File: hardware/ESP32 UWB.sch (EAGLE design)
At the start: 55 parts, among them J2 HEADER-12P-2.54, J4 10118194-0001LF, Q3 S8050, Q4 S8050, U1 SILICON_LABS_CP2102N-A01-GQFN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, U2 V_REG_MIC2920, U5 DWM1000, U6 ESP32-C3-MINI-1-N4

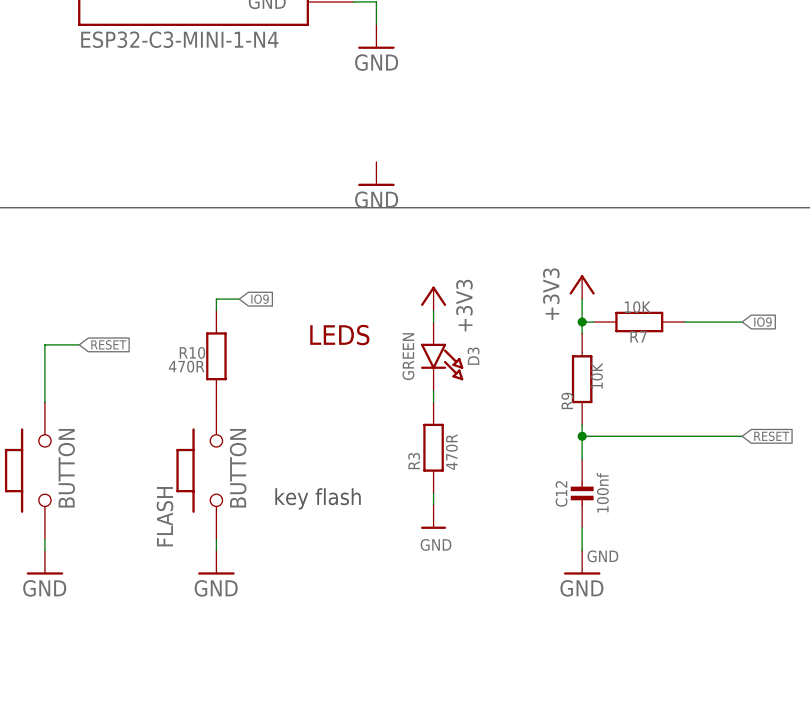
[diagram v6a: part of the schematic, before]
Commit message: fixed device prefixes, removed duplicate supply symbols
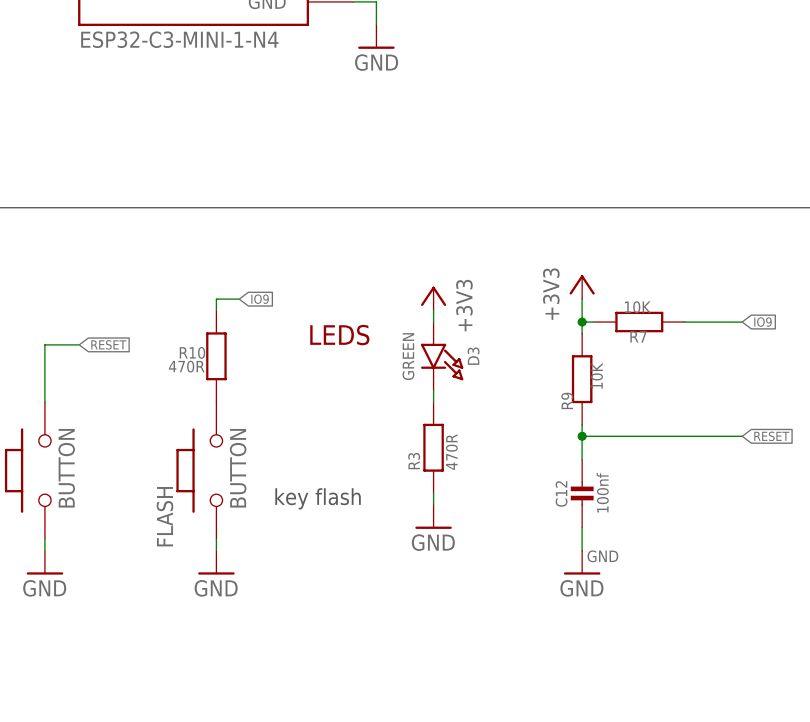
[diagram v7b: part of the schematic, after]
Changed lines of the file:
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@@
 <part name="+3V7" library="supply1" deviceset="+3V3" device=""/>
 <part name="+3V9" library="supply1" deviceset="+3V3" device=""/>
-<part name="GND13" library="supply1" deviceset="GND" device=""/>
 <part name="R18" library="isystems" deviceset="RESISTOR" device="0603" value="NC"/>
 <part name="R19" library="isystems" deviceset="RESISTOR" device="0603" value="NC"/>
@@
 <part name="GND29" library="supply1" deviceset="GND" device=""/>
 <part name="+3V4" library="supply1" deviceset="+3V3" device=""/>
-<part name="U$3" library="microbuilder" deviceset="GND" device=""/>
+<part name="U$3" library="supply1" deviceset="GND" device=""/>
 <part name="GND7" library="SparkFun-Aesthetics" deviceset="GND" device=""/>
 <part name="+3V1" library="supply1" deviceset="+3V3" device=""/>
-<part name="GND9" library="SparkFun-Aesthetics" deviceset="GND" device=""/>
+<part name="GND9" library="supply1" deviceset="GND" device=""/>
 <part name="GND10" library="SparkFun-Aesthetics" deviceset="GND" device=""/>
 <part name="R7" library="isystems" deviceset="RESISTOR" device="0603" value="10K"/>
@@
 <part name="+3V16" library="supply1" deviceset="+3V3" device=""/>
 <part name="GND45" library="SparkFun" deviceset="GND" device=""/>
-<part name="GND46" library="SparkFun" deviceset="GND" device=""/>
+<part name="GND46" library="supply1" deviceset="GND" device=""/>
 <part name="R8" library="isystems" deviceset="RESISTOR" device="0603" value="1K"/>
 <part name="R13" library="isystems" deviceset="RESISTOR" device="0603" value="1K"/>
 <part name="R14" library="isystems" deviceset="RESISTOR" device="0603" value="1K"/>
 <part name="R15" library="isystems" deviceset="RESISTOR" device="0603" value="10K"/>
-<part name="GND11" library="SparkFun" deviceset="GND" device=""/>
+<part name="GND11" library="supply1" deviceset="GND" device=""/>
 <part name="R20" library="isystems" deviceset="RESISTOR" device="0603" value="470R"/>
 <part name="D1" library="microbuilder" deviceset="LED" device="0805_NOOUTLINE" value="GREEN"/>
-<part name="GND16" library="SparkFun" deviceset="GND" device=""/>
+<part name="GND16" library="supply1" deviceset="GND" device=""/>
 <part name="R21" library="isystems" deviceset="RESISTOR" device="0603" value="470R"/>
 <part name="D2" library="microbuilder" deviceset="LED" device="0805_NOOUTLINE" value="GREEN"/>
@@
 <part name="GND15" library="supply1" deviceset="GND" device=""/>
 <part name="+3V8" library="supply1" deviceset="+3V3" device=""/>
-<part name="GND1" library="SparkFun-Aesthetics" deviceset="GND" device=""/>
+<part name="GND1" library="supply1" deviceset="GND" device=""/>
 <part name="U1" library="Silicon Labs - CP2102N-A01-GQFN28" deviceset="SILICON_LABS_CP2102N-A01-GQFN28" device="SILICON_LABS_CP2102N-A01-GQFN28_0_3" value="SILICON_LABS_CP2102N-A01-GQFN28SILICON_LABS_CP2102N-A01-GQFN28_0_3"/>
-<part name="GND3" library="SparkFun-Aesthetics" deviceset="GND" device=""/>
+<part name="GND3" library="supply1" deviceset="GND" device=""/>
 <part name="U$8" library="microbuilder" deviceset="VBUS" device=""/>
 <part name="R1" library="isystems" deviceset="RESISTOR" device="0603" value="470R"/>
@@
 <part name="D9" library="SparkFun-LED" deviceset="WS2812B" device="" value="WS2812B"/>
 <part name="GND4" library="supply1" deviceset="GND" device=""/>
-<part name="GND5" library="SparkFun-Aesthetics" deviceset="GND" device=""/>
+<part name="GND5" library="supply1" deviceset="GND" device=""/>
 <part name="SJ1" library="isystems" deviceset="SJ" device="S"/>
 </parts>
@@
 <instance part="+3V7" gate="G$1" x="304.8" y="45.72"/>
 <instance part="+3V9" gate="G$1" x="309.88" y="45.72"/>
-<instance part="GND13" gate="1" x="210.82" y="55.88" rot="MR0"/>
 <instance part="R18" gate="G$1" x="299.72" y="36.83" smashed="yes" rot="R270">
 <attribute name="NAME" x="299.72" y="31.75" size="1.27" layer="95" font="vector" rot="R270"/>
@@
 <instance part="GND29" gate="1" x="193.04" y="12.7"/>
 <instance part="+3V4" gate="G$1" x="217.17" y="44.45" rot="MR0"/>
-<instance part="U$3" gate="G$1" x="217.17" y="17.78"/>
+<instance part="U$3" gate="1" x="217.17" y="17.78"/>
 <instance part="GND7" gate="1" x="226.06" y="91.44"/>
 <instance part="+3V1" gate="G$1" x="137.16" y="116.84"/>
@@
 <segment>
 <pinref part="R3" gate="G$1" pin="1"/>
-<pinref part="U$3" gate="G$1" pin="GND"/>
+<pinref part="U$3" gate="1" pin="GND"/>
 <wire x1="217.17" y1="21.59" x2="217.17" y2="20.32" width="0.1524" layer="91"/>
 </segment>

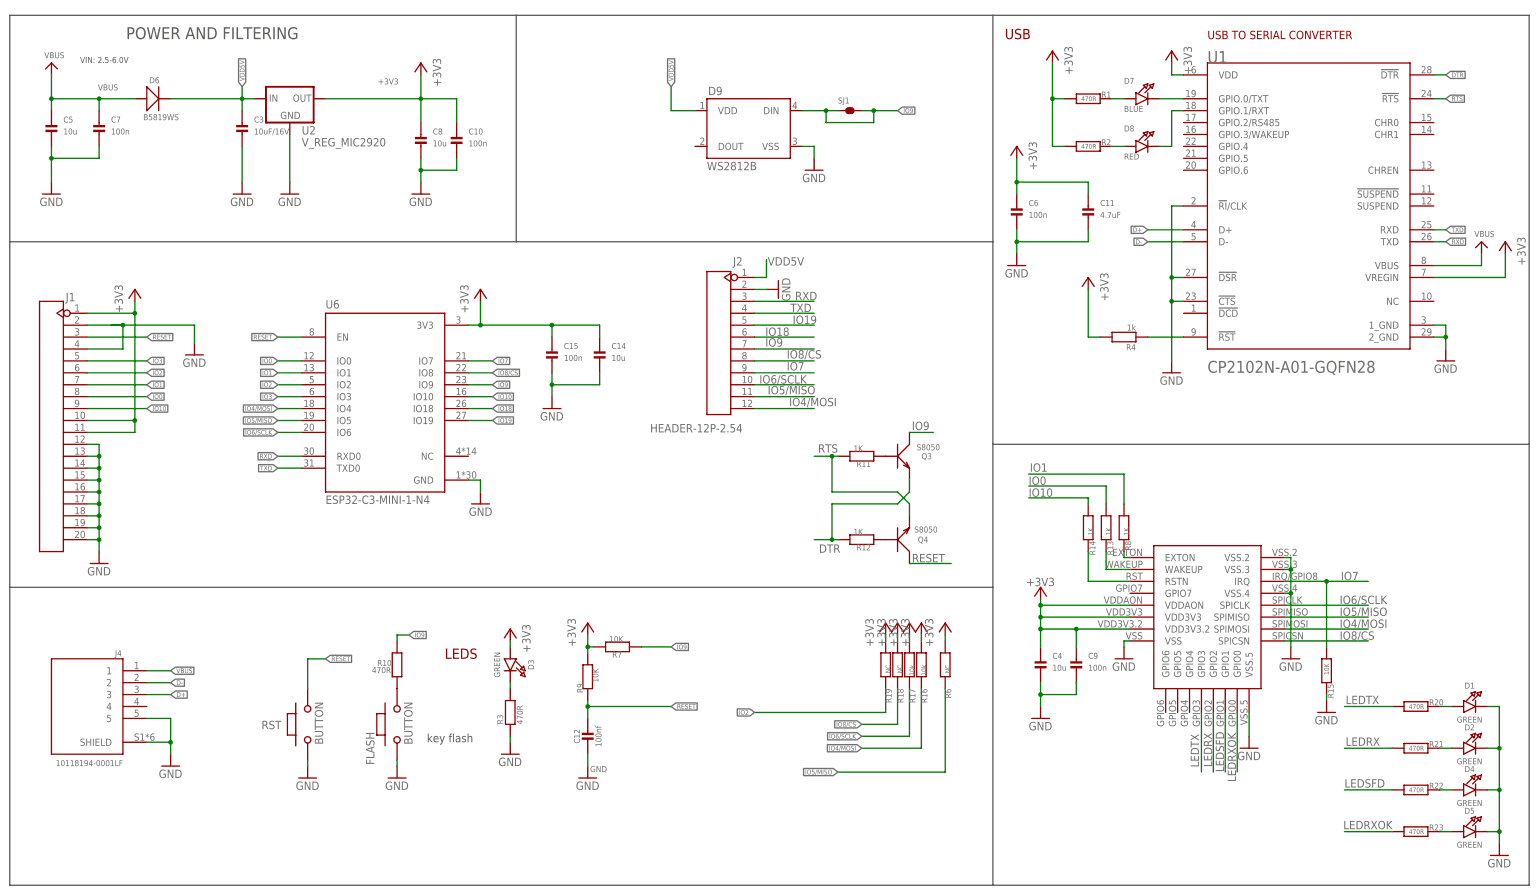
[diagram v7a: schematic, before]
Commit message: renumbered parts
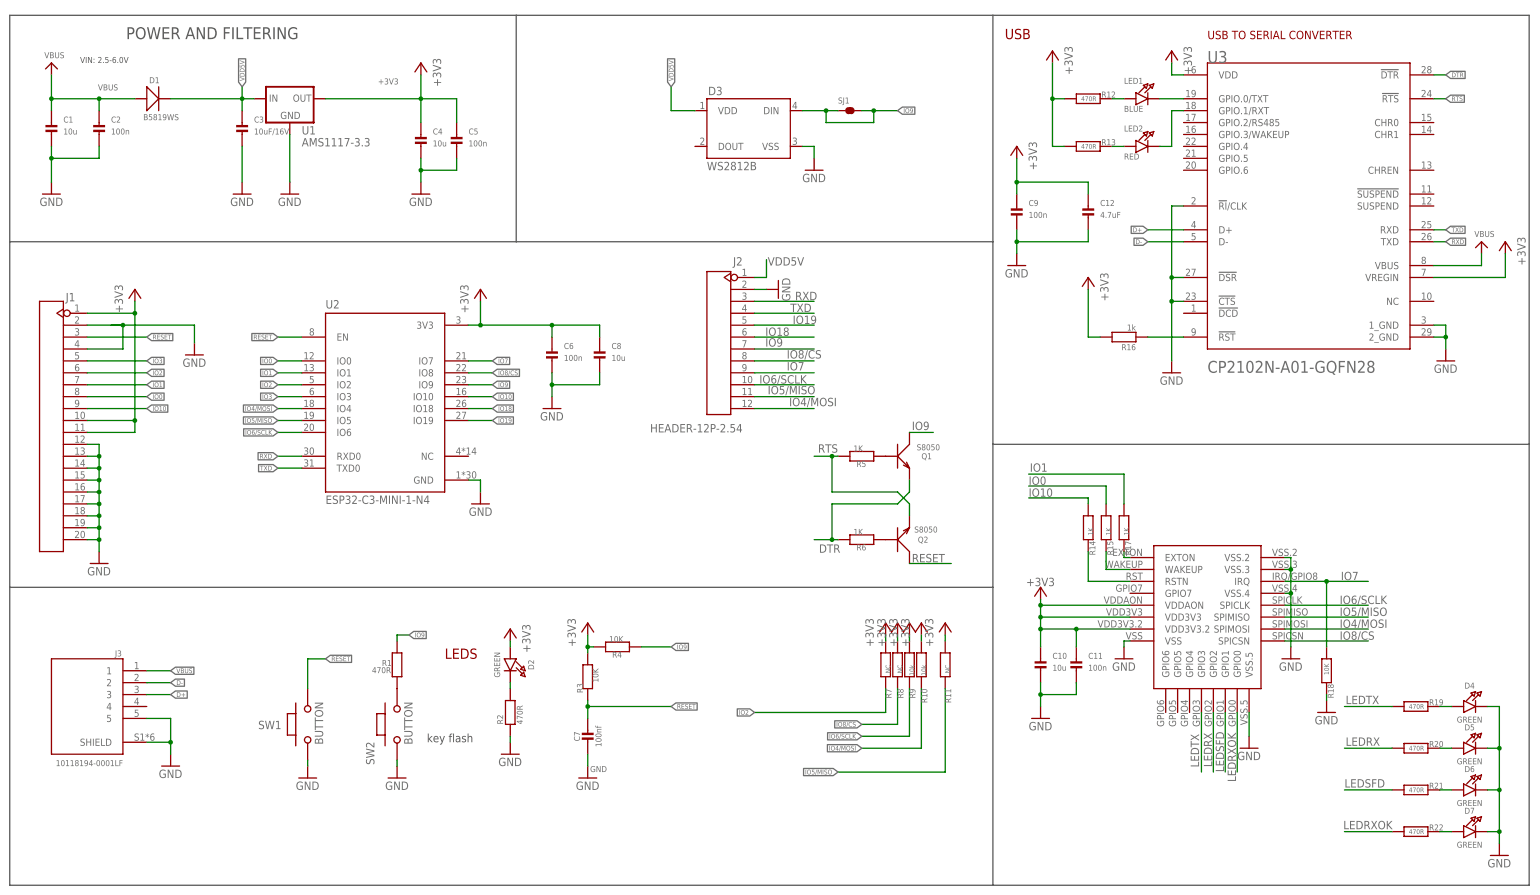
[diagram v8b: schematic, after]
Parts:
- removed C14: 10u, isystems:CAP_CERAMIC0603
- removed C15: 100n, isystems:CAP_CERAMIC0603
- removed D9: WS2812B, SparkFun-LED:WS2812B
- removed R23: 470R, isystems:RESISTOR0603
- removed U6: ESP32-C3-MINI-1-N4, ESP32-C3-MINI-1-N4:ESP32-C3-MINI-1-N4
- added C1: 10u, isystems:CAP_CERAMIC0603
- added C2: 100n, isystems:CAP_CERAMIC0603
- added LED1: BLUE, isystems:LED0603_NOOUTLINE
- added R5: 1K, isystems:RESISTOR0603
- added U3: SILICON_LABS_CP2102N-A01-GQFN28SILICON_LABS_CP2102N-A01-GQF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, Silicon Labs - CP2102N-A01-GQFN28:SILICON_LABS_CP2102N-A01-GQFN28SILICON_LABS_CP2102N-A01-GQFN28_0_3
- C10: value 100n -> 10u
- C11: value 4.7uF -> 100n
- C12: value 100nf -> 4.7uF; device microbuilder:CAP_CERAMIC0603_NO -> isystems:CAP_CERAMIC0603
- C5: value 10u -> 100n
- C7: value 100n -> 100nf; device isystems:CAP_CERAMIC0603 -> microbuilder:CAP_CERAMIC0603_NO
- D1: value GREEN -> B5819WS; device microbuilder:LED0805_NOOUTLINE -> Discrete:D'0805'
- D3: value GREEN -> WS2812B; device microbuilder:LED0805_NOOUTLINE -> SparkFun-LED:WS2812B
- D6: value B5819WS -> GREEN; device Discrete:D'0805' -> microbuilder:LED0805_NOOUTLINE
- D7: value BLUE -> GREEN; device isystems:LED0603_NOOUTLINE -> microbuilder:LED0805_NOOUTLINE
- R10: value 470R -> 10k
- R11, R8: value 1K -> NC
- R12, R13: value 1K -> 470R
- R15: value 10K -> 1K
- R16: value 10k -> 1k
- R17: value 10k -> 1K
- R18: value NC -> 10K
- R19: value NC -> 470R
- R3: value 470R -> 10K
- R4: value 1k -> 10K
- R6: value NC -> 1K
- R7: value 10K -> NC
- R9: value 10K -> 10k
- U1: value SILICON_LABS_CP2102N-A01-GQFN28SILICON_LABS_CP2102N-A01-GQFN28_0_3 -> AMS1117-3.3; device Silicon Labs - CP2102N-A01-GQFN28:SILICON_LABS_CP2102N-A01-GQFN28SILICON_LABS_CP2102N-A01-GQFN28_0_3 -> SparkFun-PowerIC:V_REG_MIC2920
- U2: value V_REG_MIC2920 -> ESP32-C3-MINI-1-N4; device SparkFun-PowerIC:V_REG_MIC2920 -> ESP32-C3-MINI-1-N4:ESP32-C3-MINI-1-N4
- renumbered D8 to LED2, FLASH to SW2, J4 to J3, Q3 to Q1, Q4 to Q2, RST to SW1, U5 to U4
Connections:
- net +3V3: now also C12.P$1, C5.P$1, D2.A, R10.1, R11.1, R12.1, R13.1, R16.2, R3.2, R7.1, R8.1, R9.1, U1.OUT, U2.3V3, U3.VDD, U3.VREGIN; no longer C14.P$1, C15.P$1, D3.A, R1.1, R16.1, R17.1, R18.1, R19.1, R2.1, R6.1, R7.2, R9.2, U1.VDD, U1.VREGIN, U2.OUT, U6.3V3
- net D+: now also U3.D+; no longer U1.D+
- net D-: now also U3.D-; no longer U1.D-
- net DTR: now also R6.2, U3.!DTR!; no longer R12.2, U1.!DTR!
- net GND: now also C1.P$2, C12.P$2, C2.P$2, C7.2, D3.VSS, D6.C, D7.C, R18.2, R2.1, U1.GND, U3.!CTS!, U3.!DSR!, U3.!RI!/CLK, U3.1_GND, U3.2_GND; no longer C12.2, C14.P$2, C15.P$2, C7.P$2, D1.C, D2.C, D9.VSS, R15.2, R3.1, U1.!CTS!, U1.!DSR!, U1.!RI!/CLK, U1.1_GND, U1.2_GND, U6.GND
- net IO0: now also R15.1, U2.IO0; no longer R13.1, U6.IO0
- net IO1: now also R17.1, U2.IO1; no longer R8.1, U6.IO1
- net IO10: now also U2.IO10; no longer U6.IO10
- net IO18: now also U2.IO18; no longer U6.IO18
- net IO19: now also U2.IO19; no longer U6.IO19
- net IO2: now also R7.2, U2.IO2; no longer R19.2, U6.IO2
- net IO3: now also U2.IO3; no longer U6.IO3
- net IO4/MOSI: now also R10.2, U2.IO4; no longer R16.2, U6.IO4
- net IO5/MISO: now also R11.2, U2.IO5; no longer R6.2, U6.IO5
- net IO6/SCLK: now also R9.2, U2.IO6; no longer R17.2, U6.IO6
- net IO7: now also R18.1, U2.IO7; no longer R15.1, U6.IO7
- net IO8/CS: now also R8.2, U2.IO8; no longer R18.2, U6.IO8
- net IO9: now also D3.DIN, R1.2, R4.1, U2.IO9; no longer D9.DIN, R10.2, R7.1, U6.IO9
- net LEDRX: now also R20.1; no longer R21.1
- net LEDRXOK: now also R22.1; no longer R23.1
- net LEDSFD: now also R21.1; no longer R22.1
- net LEDTX: now also R19.1; no longer R20.1
- net N$1: now also D4.A, R19.2; no longer D1.A, R20.2
- net N$10: now also R17.2; no longer R8.2
- net N$11: now also R15.2; no longer R13.2
- net N$13: now also R6.1; no longer R12.1
- net N$14: now also R5.1; no longer R11.1
- net N$15: now also R1.1; no longer R10.1
- net N$16: now also D5.A, R20.2; no longer D2.A, R21.2
- net N$17: now also D6.A, R21.2; no longer D4.A, R22.2
- net N$18: now also D7.A, R22.2; no longer D5.A, R23.2
- net N$2: now also LED1.A, R12.2; no longer D7.A, R1.2
- net N$3: now also LED1.C, U3.GPIO.0/TXT; no longer D7.C, U1.GPIO.0/TXT
- net N$4: now also R13.2; no longer R2.2
- net N$5: now also D2.C, R2.2; no longer D3.C, R3.2
- net N$6: now also U3.GPIO.1/RXT; no longer U1.GPIO.1/RXT
- net N$8: now also R16.1, U3.!RST!; no longer R4.1, U1.!RST!
- net RESET: now also C7.1, R3.1, U2.EN; no longer C12.1, R9.1, U6.EN
- net RTS: now also R5.2, U3.!RTS!; no longer R11.2, U1.!RTS!
- net RXD: now also U2.RXD0, U3.TXD; no longer U1.TXD, U6.RXD0
- net TXD: now also U2.TXD0, U3.RXD; no longer U1.RXD, U6.TXD0
- net VBUS: now also C1.P$1, C2.P$1, D1.+, U3.VBUS; no longer C5.P$1, C7.P$1, D6.+, U1.VBUS
- net VDD5V: now also D1.-, D3.VDD, U1.IN; no longer D6.-, D9.VDD, U2.IN
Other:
- moved on the sheet: C10, C11, C12, C4, C5, C6, C7, C8, C9, D2, D4, D5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
